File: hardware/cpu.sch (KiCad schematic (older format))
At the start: 77 parts, among them J801 HANDSFREE, J802 microphone, J803 HEADPHONES, P801 TX_SW_WIRE, Q801 Q_PMOS_DGS, SW801 SW_PUSH, SW802 SW, SW803 SW, SW804 SW, SW805 SW, SW806 SW, SW807 SW, SW808 encoder, SW809 encoder, U801 STM32F401, U802 WM8731

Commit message: Upgraded schematic to version 1.0 and generated initial BOM
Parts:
- removed C810: 1µF, symbol CP
- removed C811, C812, C820, C821, C823: 10µF, symbol CP
- added C808, C811: 10µF, symbol C
- added D802: PMEG6020EP, symbol D_Schottky
- added P802: USB_B, symbol USB_B
- added P803: UART, symbol CONN_01X02
- added P804: PROG, symbol CONN_01X02
- added P805: RNG_PINS, symbol CONN_02X08
- added P806: CONN_01X08, symbol CONN_01X08
- added P807: CONN_01X04, symbol CONN_01X04
- added P808: CONN_02X04, symbol CONN_02X04
- added P809: BOOT0JMPR, symbol CONN_02X01
- added R807: 10k, symbol R
- added R819: 50R, symbol R
- added R820, R821: 1k, symbol R
- added SW807: RESET, symbol SW_PUSH_SMALL
- C803: value 4.7µF -> 10µF
- C812: renamed from C813; value 0.1µF -> 10µF
- C813: renamed from C814; value 0.1µF -> 10µF
- C814: renamed from C815; value 0.1µF -> 10µF
- C815: renamed from C816; value 0.1µF -> 10µF
- C817: renamed from C819; value 10nF -> 1nF
- C818: value 0.1µF -> 10µF
- C820: renamed from C824; value 10nF -> 1nF
- R805: value 1k -> 10k
- renumbered C807 to C806, C806 to C807, C808 to C809, C809 to C810, C817 to C816, C822 to C819, D802 to D803, D803 to D804, D807 to D805, D808 to D806, D809 to D807, D804 to D808, D810 to D809, D811 to D810, D805 to D811, D816 to D814, D814 to D815, D806 to D816, D815 to D817, R809 to R808, R807 to R809, R813 to R811, R814 to R812, R808 to R813, R815 to R814, R816 to R815, R817 to R816, R811 to R817, R812 to R818, R818 to R822, SW805 to SW802, SW806 to SW803, SW807 to SW804, SW802 to SW805, SW808 to SW806, SW803 to SW808, SW804 to SW810
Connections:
- net labels added: CPURST, PA11/USB, PA12/USB, PA2, PA3, PB10, PB2, PB3/SWO, PC13, PC15, PC3, PD2, PH0, PH1, SWCLK, SWDIO, UART_RX, UART_TX, UI_SW_GRID1, UI_SW_GRID2, UI_SW_GRID3, UI_SW_GRID4, Vin
- wire segments 227 -> 349
- no-connect marks 29 -> 10
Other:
- note added: "TANGENTTI"
- note added: "TX_RX_SW_OUT"
- note added: "connector block"
- note removed: "SPI"
- note removed: "USB"
- note removed: "rx"
- note removed: "screen backlight"
- note removed: "tx"
- note removed: "uart"
- moved on the sheet: C806, C812, C813, C816, C817, C819, C820, D805, D806, D807, D808, D809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

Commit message: Linked first components to footprints and updated schematic plot
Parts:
- C801, C802, C803, C804, C805, C806, C807, C808, C809, C810, C811, C812, C813, C814, C815, C816, C817, C818, C819, C820: footprint (none) -> Capacitors_SMD:C_0805
- D801, D803, D804: footprint (none) -> TO_SOT_Packages_SMD:SOT-23_Handsoldering
- D802: footprint (none) -> Diodes_SMD:SOD-523
- P802: footprint (none) -> Connect:USB_B
- P803, P804, P809: footprint (none) -> Pin_Headers:Pin_Header_Straight_1x02
- P805: footprint (none) -> Pin_Headers:Pin_Header_Straight_2x08
- P806: footprint (none) -> Pin_Headers:Pin_Header_Straight_1x08
- P807: footprint (none) -> Pin_Headers:Pin_Header_Straight_1x04
- P808: footprint (none) -> Pin_Headers:Pin_Header_Straight_2x04
- R801, R802, R803, R804, R805, R806, R807, R808, R809, R810, R811, R812, R813, R814, R815, R816, R817, R818, R819, R820, R821: footprint (none) -> Resistors_SMD:R_0805_HandSoldering
- U801: footprint (none) -> Housings_QFP:LQFP-64_10x10mm_Pitch0.5mm
- U802: footprint (none) -> Housings_SSOP:SSOP-28_5.3x10.2mm_Pitch0.65mm

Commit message: Added more electrical protections
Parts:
- added D818, D819, D820, D821, D822, D823: BAT54, symbol D_Schottky_x2_Serial_AKC
- added R823, R824, R829: 50R, symbol R
- added R825, R826, R827, R828, R830, R831, R832, R833, R834, R835: 1k, symbol R
- C804: value 10µF -> 1n
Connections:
- wire segments 349 -> 386
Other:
- moved on the sheet: C804, P801, P803, P804, P805, R801, R802, SW801

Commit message: Changed SWR microstrip for two transformers and gave missing values for components
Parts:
- removed P802: USB_B, Connect:USB_B, symbol USB_B
- added P?: USB_OTG, symbol USB_OTG
- C802: value C -> 1nF
- D805, D806, D807, D808, D809, D810, D811, D812, D813, D815, D816, D817: value D -> 1N914
- Q801: value Q_PMOS_DGS -> BSS84
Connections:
- no-connect marks 10 -> 11
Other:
- moved on the sheet: D802

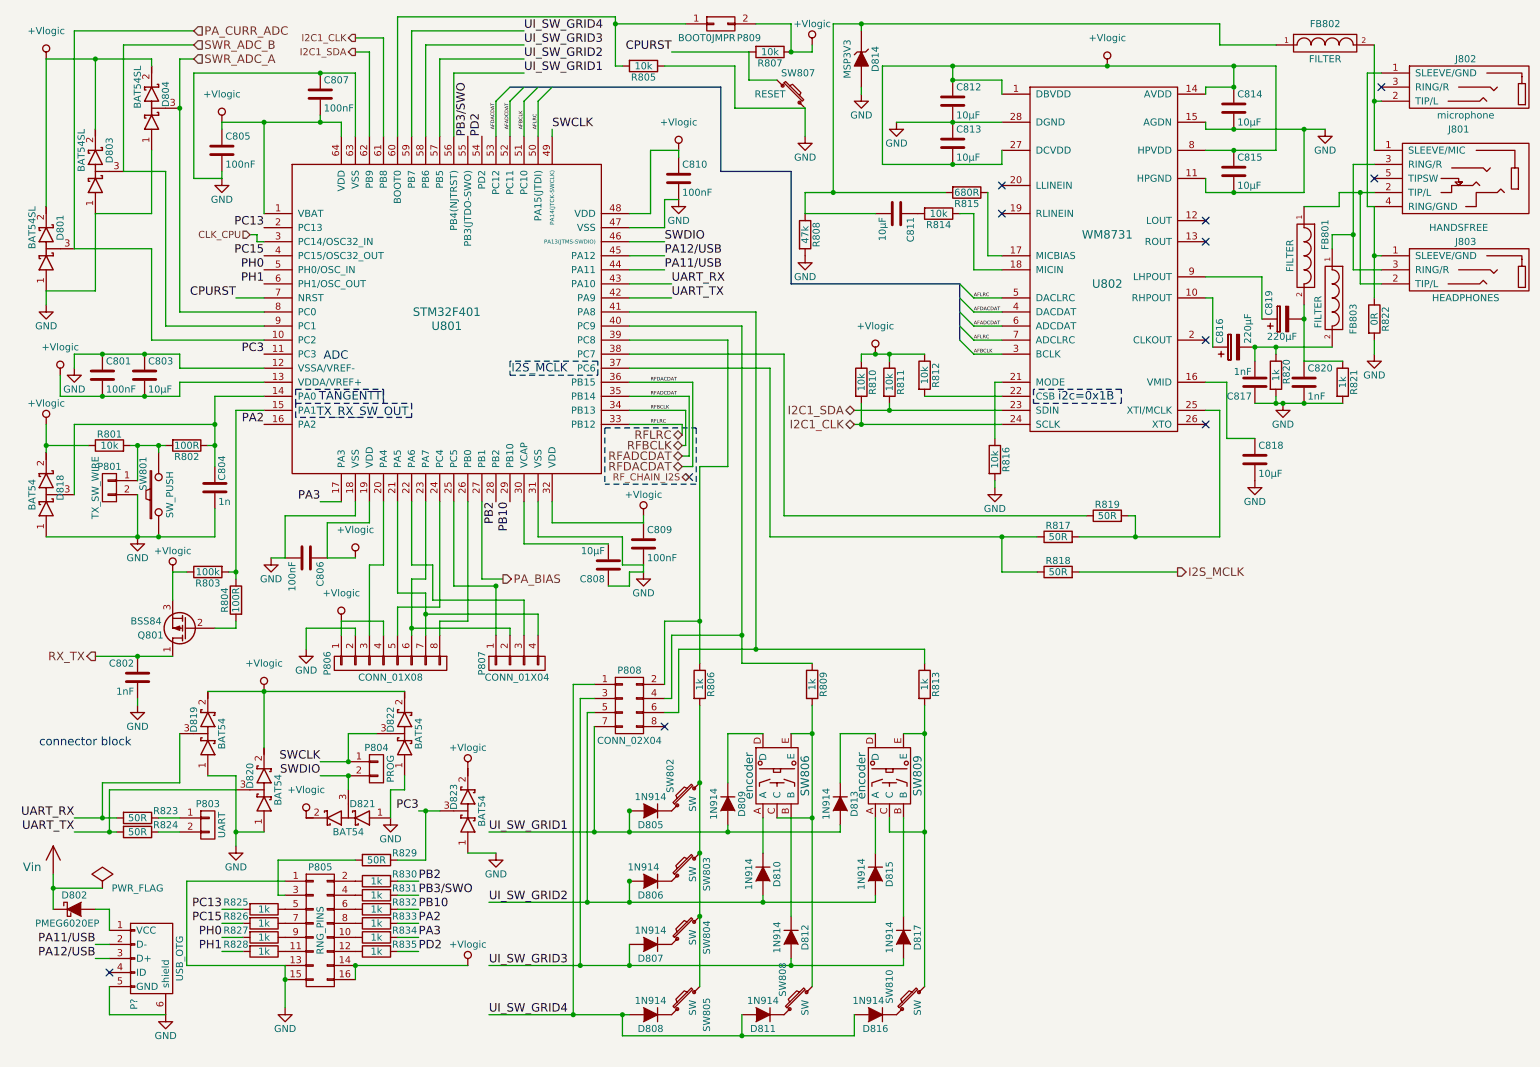
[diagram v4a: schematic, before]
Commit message: Fixed some bugs and annotated rest of the footprints
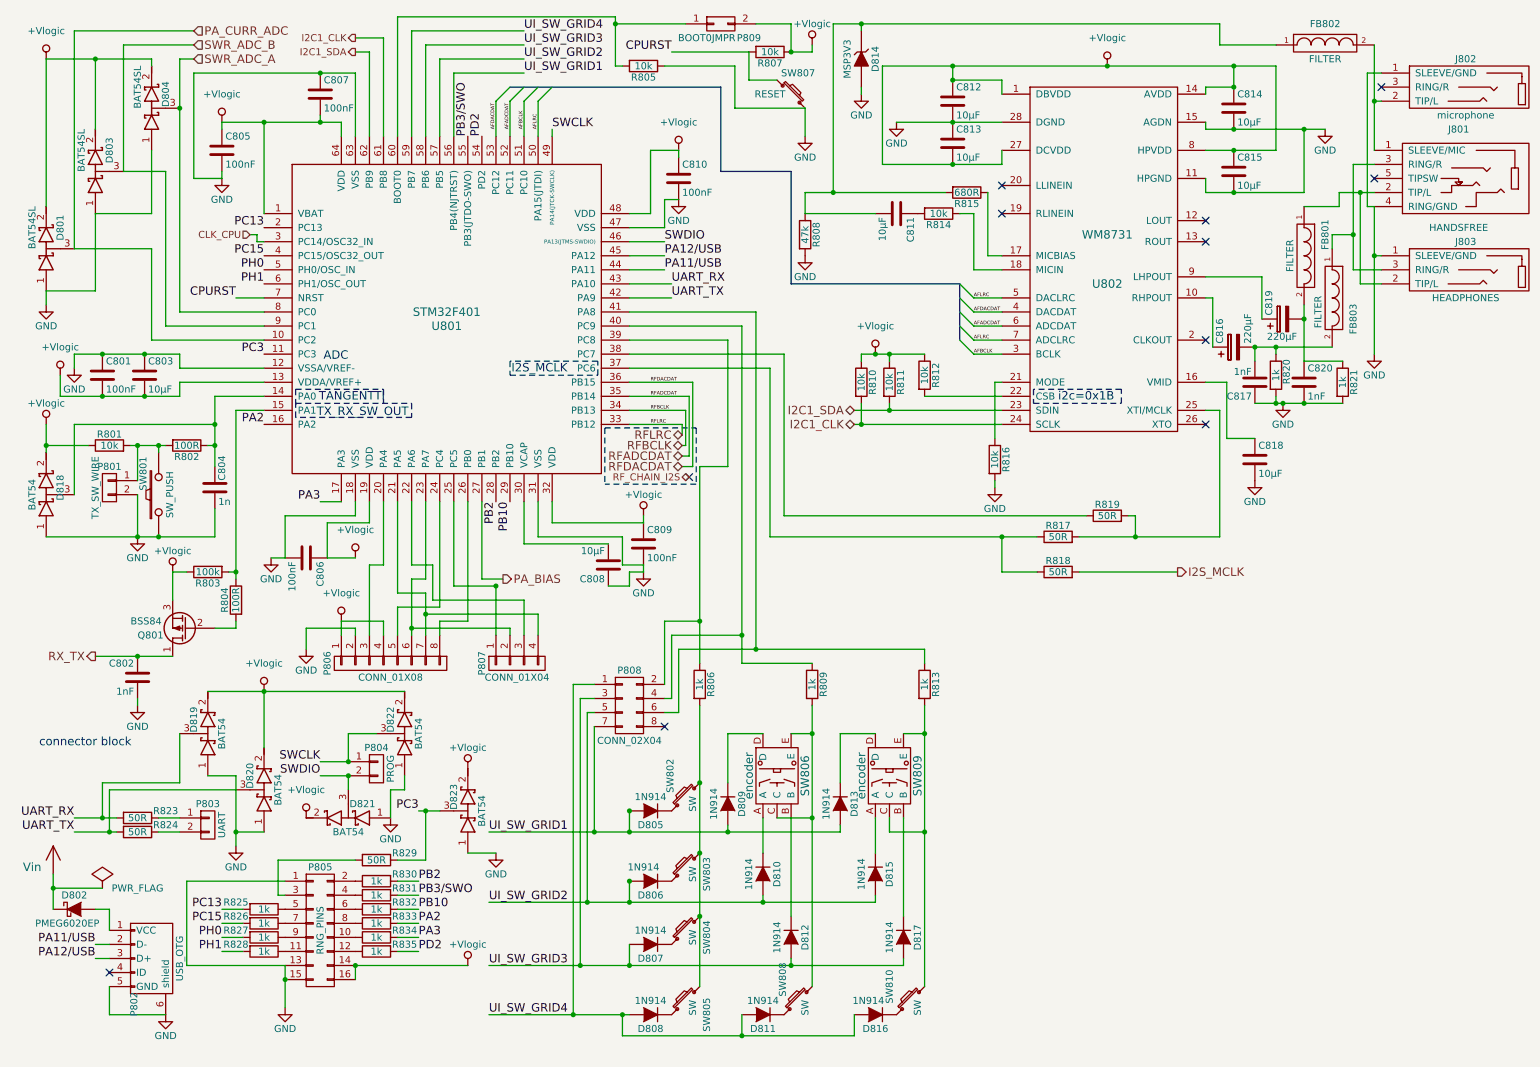
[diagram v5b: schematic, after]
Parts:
- removed R822: 0R, symbol R
- C801, C802, C803, C804, C805, C806, C807, C808, C809, C810, C811, C812, C813, C814, C815, C817, C818, C820: footprint Capacitors_SMD:C_0805 -> Capacitors_SMD:C_0805_HandSoldering
- C816, C819: footprint Capacitors_SMD:C_0805 -> dodekaedri:CAP_6.3x5.8mm
- D805, D806, D807, D808, D809, D810, D811, D812, D813, D815, D816, D817, D818, D819, D820, D821, D822, D823, Q801: footprint (none) -> TO_SOT_Packages_SMD:SOT-23_Handsoldering
- D814: footprint (none) -> dodekaedri:Micro_SMP
- FB801, FB802, FB803, R823, R824, R825, R826, R827, R828, R829, R830, R831, R832, R833, R834, R835: footprint (none) -> Resistors_SMD:R_0805_HandSoldering
- J801: footprint (none) -> dodekaedri:TRRS_jack
- J802, J803: footprint (none) -> dodekaedri:TRS_jack
- P801: footprint (none) -> Connect:AK300-2
- P802: renamed from P?; footprint (none) -> Connect:USB_Micro-B
- SW801, SW802, SW803, SW804, SW805, SW807, SW808, SW810: footprint (none) -> Buttons_Switches_SMD:SW_SPST_B3SL-1002P
- SW806, SW809: footprint (none) -> dodekaedri:encoder
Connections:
- net GND: now also J801.4 (RING/GND), J802.1 (SLEEVE/GND), J803.1 (SLEEVE/GND)

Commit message: recommit before doing drastic netlist changes?
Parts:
- D802: footprint Diodes_SMD:SOD-523 -> Diodes_SMD:D_0805
- SW806, SW809: symbol encoder -> encoder-RESCUE-dodekaedri
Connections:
- net at R809.2, SW808.2: now also SW806.~ (E); no longer SW806.C, SW806.E
- net at R813.2, SW810.2: now also SW809.~ (E); no longer SW809.C, SW809.E
- net at D809.1 (K): now also SW806.~ (E); no longer SW806.D
- net at D812.1 (K): now also SW806.~ (E); no longer SW806.B
- net at D810.1 (K): now also SW806.~ (E); no longer SW806.A
- net at D813.1 (K): now also SW809.~ (E); no longer SW809.D
- net at D817.1 (K): now also SW809.~ (E); no longer SW809.B
- net at D815.1 (K): now also SW809.~ (E); no longer SW809.A
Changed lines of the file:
@@
 EESchema Schematic File Version 2
+LIBS:dodekaedri-rescue
 LIBS:power
 LIBS:device
@@
 $EndComp
 $Comp
-L encoder SW806
+L encoder-RESCUE-dodekaedri SW806
 U 1 1 57EB2E07
 P 5850 5900
+AR Path="/57EB2E07" Ref="SW806"  Part="1"
+AR Path="/57E5C816/57EB2E07" Ref="SW806"  Part="1"
 F 0 "SW806" V 6050 5900 60  0000 C CNN
 F 1 "encoder" V 5650 5900 60  0000 C CNN
@@
 $EndComp
 $Comp
-L encoder SW809
+L encoder-RESCUE-dodekaedri SW809
 U 1 1 57EB76AB
 P 6650 5900
+AR Path="/57EB76AB" Ref="SW809"  Part="1"
+AR Path="/57E5C816/57EB76AB" Ref="SW809"  Part="1"
 F 0 "SW809" V 6850 5900 60  0000 C CNN
 F 1 "encoder" V 6450 5900 60  0000 C CNN
@@
 F 0 "D802" H 850 6950 50  0000 C CNN
 F 1 "PMEG6020EP" H 800 6750 50  0000 C CNN
-F 2 "Diodes_SMD:SOD-523" H 850 6850 50  0001 C CNN
+F 2 "Diodes_SMD:D_0805" H 850 6850 50  0001 C CNN
 F 3 "" H 850 6850 50  0000 C CNN
 	1    850  6850

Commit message: failsafe commit just before recreating netlist
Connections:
- net CLK_CPU: now also U801.5 (PH0/OSC_IN); no longer U801.3 (PC14/OSC32_IN)
- net PC13: now also R826.2; no longer R825.2
- net PC15: now also R827.2; no longer R826.2
- removed net PH0: R827.2, U801.5 (PH0/OSC_IN)
- new net PC14: R825.2, U801.3 (PC14/OSC32_IN)
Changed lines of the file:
@@
 Text HLabel 5225 3775 0    50   BiDi ~ 0
 RF_CHAIN_I2S
-Text HLabel 2100 2050 0    50   Input ~ 0
+Text HLabel 2050 2250 0    50   Input ~ 0
 CLK_CPU
 Text Notes 2800 2950 2    60   ~ 0
@@
 	2200 3100 1600 3100
 Wire Wire Line
-	1600 3100 1600 3200
-Wire Wire Line
-	1600 3200 750  3200
+	1600 3200 1600 3100
+Wire Wire Line
+	750  3200 1600 3200
 Wire Wire Line
 	750  3200 750  3050
@@
 Connection ~ 9100 1300
 Wire Wire Line
-	9400 850  9400 1450
-Wire Wire Line
-	9400 1450 8900 1450
+	9400 1450 9400 850
+Wire Wire Line
+	8900 1450 9400 1450
 Connection ~ 9100 850
 Connection ~ 9100 1450
@@
 	8900 3300 9000 3300
 Wire Wire Line
-	9000 3300 9000 4200
+	9000 4200 9000 3300
 Wire Notes Line
 	7675 3150 7675 3250
@@
 	3650 3950 3650 4800
 Wire Wire Line
-	2100 2050 2150 2050
-Wire Wire Line
-	2150 2050 2150 2100
+	2050 2250 2150 2250
+Wire Wire Line
+	2150 2250 2150 2300
 Wire Wire Line
 	1400 2150 1400 2800
@@
 	6100 5600 5950 5600
 Wire Wire Line
-	6650 6300 6900 6300
+	6900 6300 6650 6300
 Wire Wire Line
 	6900 5400 6900 7400
@@
 	7450 4450 7700 4450
 Wire Wire Line
-	9000 4200 8000 4200
+	8000 4200 9000 4200
 Wire Wire Line
 	8050 4050 5900 4050
@@
 	5950 1600 5450 1600
 Wire Bus Line
-	5450 1600 5450 1000
+	5450 1000 5450 1600
 Wire Bus Line
-	5450 1000 3950 1000
+	3950 1000 5450 1000
 $Comp
 L R R807
@@
 Text Label 2200 2200 2    60   ~ 0
 PC15
-Text Label 2200 2300 2    60   ~ 0
-PH0
+Text Label 2200 2100 2    60   ~ 0
+PC14
 Text Label 2200 2400 2    60   ~ 0
 PH1
-Text Label 1900 6950 2    60   ~ 0
+Text Label 1900 7050 2    60   ~ 0
 PC15
-Text Label 1900 7050 2    60   ~ 0
-PH0
+Text Label 1900 6850 2    60   ~ 0
+PC14
 Text Label 1900 7150 2    60   ~ 0
 PH1
 Text Label 2200 2000 2    60   ~ 0
 PC13
-Wire Wire Line
-	2150 2100 2200 2100
-Text Label 1900 6850 2    60   ~ 0
+Text Label 1900 6950 2    60   ~ 0
 PC13
 Text Label 2200 2900 2    60   ~ 0
@@
 $EndComp
 NoConn ~ 1100 7300
+Wire Wire Line
+	2150 2300 2200 2300
 $EndSCHEMATC

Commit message: 15% of layout done.. hopefully
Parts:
- D808, D811, D813, D815, D816, D817: footprint TO_SOT_Packages_SMD:SOT-23_Handsoldering -> (none)
- J802, J803: footprint dodekaedri:TRS_jack -> (none)
- R813: footprint Resistors_SMD:R_0805_HandSoldering -> (none)
- SW806: symbol encoder-RESCUE-dodekaedri -> encoder
- SW808, SW810: footprint Buttons_Switches_SMD:SW_SPST_B3SL-1002P -> (none)
- SW809: footprint dodekaedri:encoder -> (none); symbol encoder-RESCUE-dodekaedri -> encoder
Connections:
- net at R809.2, SW808.2: now also SW806.C, SW806.E; no longer SW806.~ (E)
- net at R813.2, SW810.2: now also SW809.C, SW809.E; no longer SW809.~ (E)
- net at D809.1 (K): now also SW806.D; no longer SW806.~ (E)
- net at D812.1 (K): now also SW806.B; no longer SW806.~ (E)
- net at D810.1 (K): now also SW806.A; no longer SW806.~ (E)
- net at D813.1 (K): now also SW809.D; no longer SW809.~ (E)
- net at D817.1 (K): now also SW809.B; no longer SW809.~ (E)
- net at D815.1 (K): now also SW809.A; no longer SW809.~ (E)
